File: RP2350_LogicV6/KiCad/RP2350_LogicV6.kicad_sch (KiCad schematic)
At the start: 69 parts, among them J2 Conn_02x16_Odd_Even, J3 SWD, J4 USB_B_Micro, J5 2350 BOOT SEL, J6 SWD, J7 SWD, J9 VGA, U1 TXU0104PWR, U10 RP2350A-QFN60, U2 TXU0104PWR, U3 TXU0104PWR, U4 TXU0104PWR, U5 TXU0104PWR, U6 TXU0104PWR, U7 LD1117S33TR_SOT223, U8 TLV74311PDBVR, U9 W25Q16JVSSIQ, Y1 12MHz

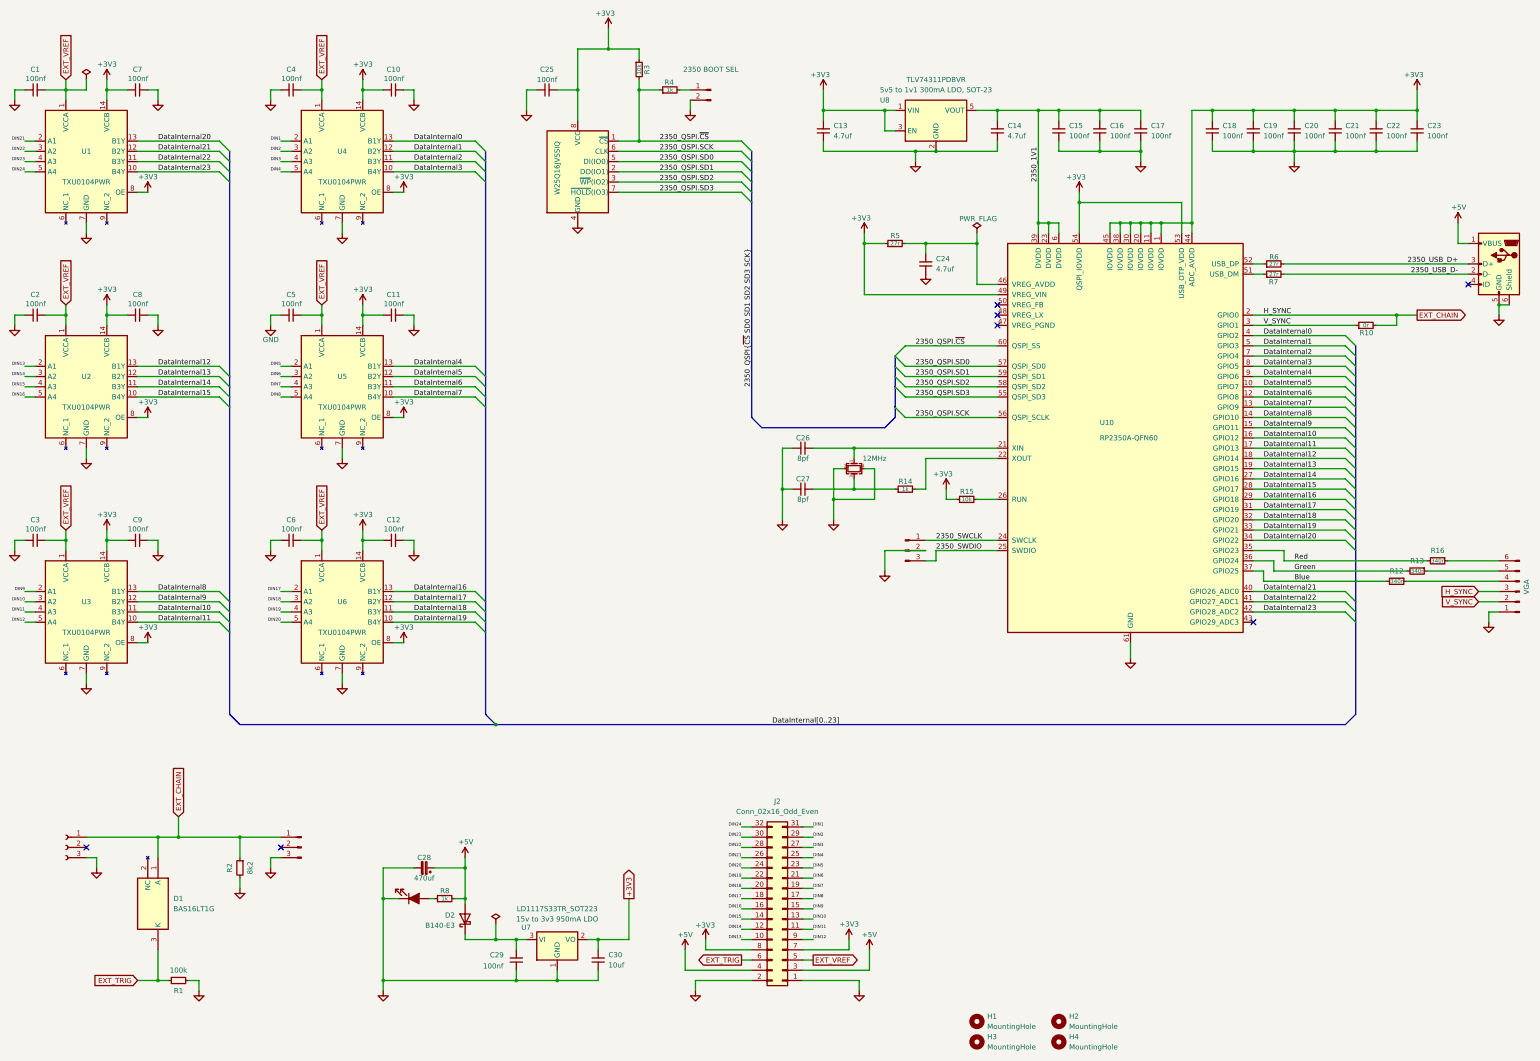
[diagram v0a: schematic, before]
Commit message: - Updated To KiCad 10
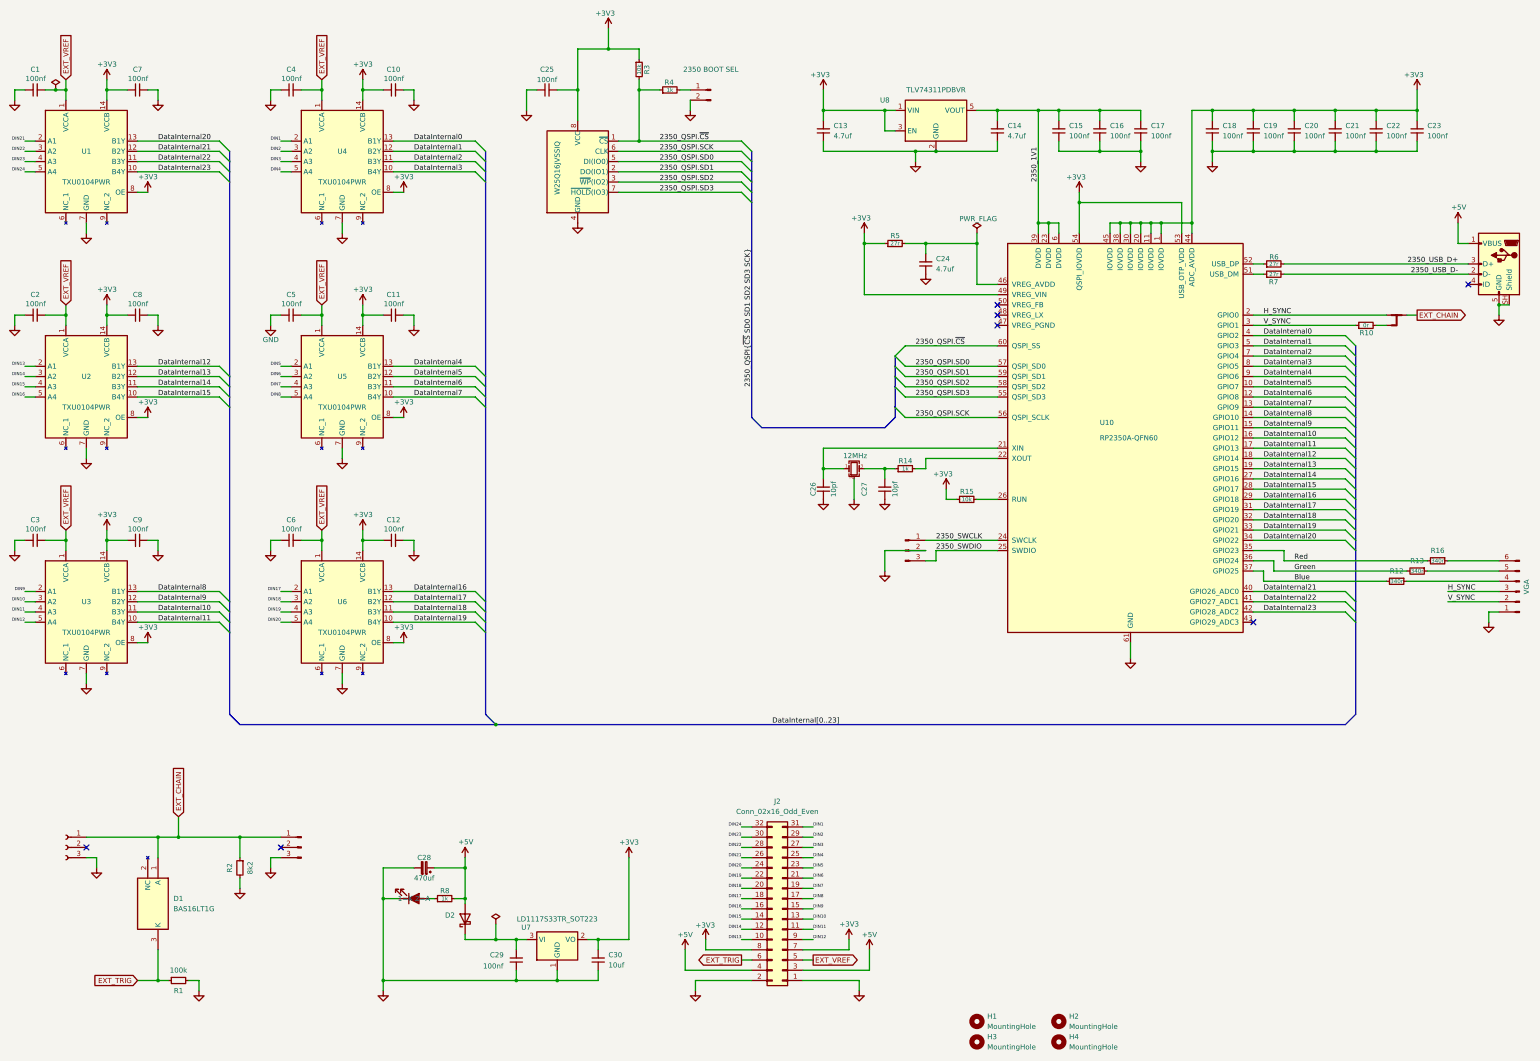
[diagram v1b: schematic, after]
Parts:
- added NT1: NetTie_3, NetTie:NetTie-3_SMD_Pad0.5mm, symbol Device:NetTie_3
- C26, C27: value 8pf -> 10pf
- D2: value B140-E3 -> (none)
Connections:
- net EXT_CHAIN: now also NT1.2; no longer J9.3 (Pin_3), R10.2, U10.2 (GPIO0)
- net GND: now also J4.SH (Shield); no longer J4.6 (Shield)
- new net: NT1.3, R10.2
- new net H_SYNC: J9.3 (Pin_3), NT1.1, U10.2 (GPIO0)
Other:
- moved on the sheet: C26, R14
